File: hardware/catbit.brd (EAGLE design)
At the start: 95 x 72 mm, 37 parts, among them J0 DC24V, Q1 60V/32A/35mΩ, Q2 60V/32A/35mΩ, Q3 60V/32A/35mΩ, Q4 60V/32A/35mΩ, Q5 60V/32A/35mΩ, Q6 60V/32A/35mΩ, Q7 60V/32A/35mΩ, Q8 60V/32A/35mΩ

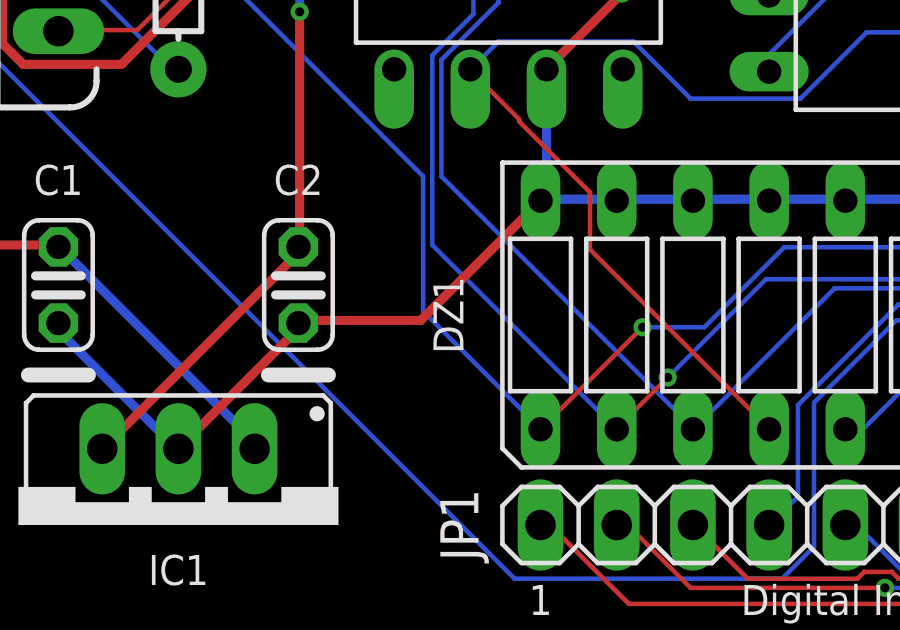
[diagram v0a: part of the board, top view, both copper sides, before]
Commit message: Renamed DZ1 to L1.
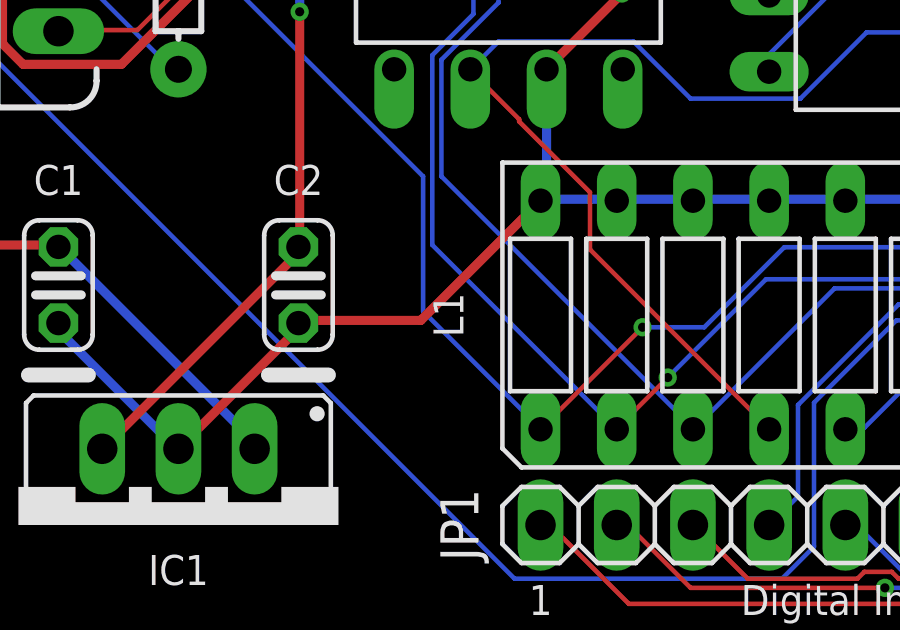
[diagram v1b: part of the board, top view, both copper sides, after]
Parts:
- renumbered DZ1 to L1
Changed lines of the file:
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@@
 <attribute name="VALUE" x="66.507" y="9.365" size="1.27" layer="27" ratio="10"/>
 </element>
-<element name="DZ1" library="led" library_urn="urn:adsk.eagle:library:259" package="LB10" package3d_urn="urn:adsk.eagle:package:15791/1" value="LB10" x="47.5" y="11" smashed="yes">
+<element name="L1" library="led" library_urn="urn:adsk.eagle:library:259" package="LB10" package3d_urn="urn:adsk.eagle:package:15791/1" value="LB10" x="47.5" y="11" smashed="yes">
 <attribute name="NAME" x="33.5" y="11" size="1" layer="25" ratio="10" rot="R90" align="bottom-center"/>
 <attribute name="POPULARITY" value="1" x="47.5" y="11" size="1.778" layer="27" display="off"/>
@@
 <contactref element="OK7" pad="3"/>
 <contactref element="OK8" pad="3"/>
-<contactref element="DZ1" pad="20"/>
-<contactref element="DZ1" pad="19"/>
-<contactref element="DZ1" pad="18"/>
-<contactref element="DZ1" pad="17"/>
-<contactref element="DZ1" pad="13"/>
-<contactref element="DZ1" pad="14"/>
-<contactref element="DZ1" pad="15"/>
-<contactref element="DZ1" pad="16"/>
+<contactref element="L1" pad="20"/>
+<contactref element="L1" pad="19"/>
+<contactref element="L1" pad="18"/>
+<contactref element="L1" pad="17"/>
+<contactref element="L1" pad="13"/>
+<contactref element="L1" pad="14"/>
+<contactref element="L1" pad="15"/>
+<contactref element="L1" pad="16"/>
 <contactref element="IC1" pad="GND"/>
 <contactref element="C1" pad="2"/>
@@
 <contactref element="OK1" pad="2"/>
 <contactref element="RN1" pad="16"/>
-<contactref element="DZ1" pad="1"/>
+<contactref element="L1" pad="1"/>
 <wire x1="39.4716" y1="10.5918" x2="36.1188" y2="7.239" width="0.1524" layer="1"/>
 <wire x1="41.529" y1="10.5918" x2="39.4716" y2="10.5918" width="0.1524" layer="16"/>
@@
 <contactref element="OK2" pad="2"/>
 <contactref element="RN1" pad="15"/>
-<contactref element="DZ1" pad="2"/>
+<contactref element="L1" pad="2"/>
 <wire x1="33.7566" y1="42.3672" x2="33.7566" y2="45.1866" width="0.1524" layer="1"/>
 <wire x1="34.671" y1="41.4528" x2="33.7566" y2="42.3672" width="0.1524" layer="1"/>
@@
 <contactref element="OK3" pad="2"/>
 <contactref element="RN1" pad="14"/>
-<contactref element="DZ1" pad="3"/>
+<contactref element="L1" pad="3"/>
 <wire x1="33.7566" y1="29.4132" x2="33.7566" y2="32.1564" width="0.1524" layer="16"/>
 <wire x1="34.671" y1="28.4988" x2="33.7566" y2="29.4132" width="0.1524" layer="16"/>
@@
 <contactref element="OK4" pad="2"/>
 <contactref element="RN1" pad="13"/>
-<contactref element="DZ1" pad="4"/>
+<contactref element="L1" pad="4"/>
 <wire x1="35.3568" y1="17.526" x2="33.7566" y2="19.1262" width="0.1524" layer="1"/>
 <wire x1="35.3568" y1="17.4498" x2="35.3568" y2="17.526" width="0.1524" layer="1"/>
@@
 <contactref element="OK5" pad="2"/>
 <contactref element="RN1" pad="12"/>
-<contactref element="DZ1" pad="5"/>
+<contactref element="L1" pad="5"/>
 <wire x1="46.863" y1="7.239" x2="46.2534" y2="7.239" width="0.1524" layer="16"/>
 <wire x1="50.1396" y1="10.5156" x2="46.863" y2="7.239" width="0.1524" layer="16"/>
@@
 <contactref element="OK6" pad="2"/>
 <contactref element="RN1" pad="11"/>
-<contactref element="DZ1" pad="6"/>
+<contactref element="L1" pad="6"/>
 <wire x1="48.8442" y1="10.3632" x2="48.8442" y2="7.239" width="0.1524" layer="1"/>
 <wire x1="52.6542" y1="14.1732" x2="48.8442" y2="10.3632" width="0.1524" layer="1"/>
@@
 <contactref element="OK7" pad="2"/>
 <contactref element="RN1" pad="10"/>
-<contactref element="DZ1" pad="7"/>
+<contactref element="L1" pad="7"/>
 <wire x1="51.3588" y1="12.4206" x2="51.3588" y2="7.239" width="0.1524" layer="1"/>
 <wire x1="52.959" y1="14.0208" x2="51.3588" y2="12.4206" width="0.1524" layer="1"/>
@@
 <contactref element="OK8" pad="2"/>
 <contactref element="RN1" pad="9"/>
-<contactref element="DZ1" pad="8"/>
+<contactref element="L1" pad="8"/>
 <wire x1="53.8734" y1="10.3632" x2="53.8734" y2="7.239" width="0.1524" layer="1"/>
 <wire x1="57.9882" y1="14.478" x2="57.6453" y2="14.1351" width="0.1524" layer="1"/>
